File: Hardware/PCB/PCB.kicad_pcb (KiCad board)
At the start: 2 copper layers, 48 parts, among them IC1 MPXV6115VC6U, IC2 MPX5100GP, J3 Programmer, J4 Power Input, J5 Relay Terminal, Q1 MMBT2222A, SW2 RotaryEncoder_Switch_MP, U2 ADS1219IPWR, U3 LP3987H-33B5, U5 R-78E5.0-1.0, U6 AP7361C-33E, U7 DS3232M, U8 DRV8871DDA

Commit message: overall design is pretty much done, starting layout and routing now
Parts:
- removed R6: 10k, Resistor_SMD:R_0603_1608Metric_Pad0.98x0.95mm_HandSolder
- added C16: 10u, Capacitor_SMD:C_0805_2012Metric_Pad1.18x1.45mm_HandSolder, F.Cu at (-68.1, 57.1)
- added C23: 0.1uF, Capacitor_SMD:C_0603_1608Metric_Pad1.08x0.95mm_HandSolder, F.Cu at (-63.5, 56.9)
- added C24: 0.1u, Capacitor_SMD:C_0603_1608Metric_Pad1.08x0.95mm_HandSolder, F.Cu at (205.5, 86.0)
- added C31: 1uF, Capacitor_SMD:C_0603_1608Metric_Pad1.08x0.95mm_HandSolder, F.Cu at (-69.0, 25.1)
- added C32: 1uF, Capacitor_SMD:C_0603_1608Metric_Pad1.08x0.95mm_HandSolder, F.Cu at (-69.0, 27.6)
- added C33: 10u, Capacitor_SMD:C_0805_2012Metric_Pad1.18x1.45mm_HandSolder, F.Cu at (-101.5, 92.5)
- added C34: 10u, Capacitor_SMD:C_0805_2012Metric_Pad1.18x1.45mm_HandSolder, F.Cu at (-80.1, 71.9)
- added C35: 0.1u, Capacitor_SMD:C_0603_1608Metric_Pad1.08x0.95mm_HandSolder, F.Cu at (-84.7, 73.7)
- added C36: 0.1u, Capacitor_SMD:C_0603_1608Metric_Pad1.08x0.95mm_HandSolder, F.Cu at (-84.7, 76.2)
- added C39: 10uF, Capacitor_SMD:C_1206_3216Metric_Pad1.33x1.80mm_HandSolder, F.Cu at (208.9, 48.0)
- added C40: 0.1uF, Capacitor_SMD:C_0603_1608Metric_Pad1.08x0.95mm_HandSolder, F.Cu at (206.9, 48.7)
- added C41: 22uF, Capacitor_SMD:C_0805_2012Metric_Pad1.18x1.45mm_HandSolder, F.Cu at (200.6, 53.3)
- added C42: 22uF, Capacitor_SMD:C_0805_2012Metric_Pad1.18x1.45mm_HandSolder, F.Cu at (198.4, 53.3)
- added C43: 10uF, Capacitor_SMD:C_1206_3216Metric_Pad1.33x1.80mm_HandSolder, F.Cu at (211.5, 48.0)
- added C44: 10uF, Capacitor_SMD:C_1206_3216Metric_Pad1.33x1.80mm_HandSolder, F.Cu at (214.0, 48.0)
- added D4: LED, LED_SMD:LED_0603_1608Metric_Pad1.05x0.95mm_HandSolder, F.Cu at (-96.8, 94.9)
- added D5: SMD110PL-TP, Diode_SMD:D_SOD-123F, F.Cu at (189.8, 100.1)
- added D6: SMD110PL-TP, Diode_SMD:D_SOD-123F, F.Cu at (185.0, 100.1)
- added D7: SMD110PL-TP, Diode_SMD:D_SOD-123F, F.Cu at (180.1, 100.1)
- added J1: DC Motor Terminal, Vendor_Footprints:TE_1985218, F.Cu at (215.6, 65.5)
- added J18: Programmer, Vendor_Footprints:61200621621, F.Cu at (-95.4, 72.8)
- added J2: Solenoid Terminal, Vendor_Footprints:PHX_16PIN_1985292, F.Cu at (181.4, 105.7)
- added PS1: TPSM84338RCJR, Vendor_Footprints:CONV_TPSM84338RCJR, F.Cu at (203.9, 50.8)
- added Q2: MMBT2222A, Package_TO_SOT_SMD:SOT-23, F.Cu at (199.4, 96.9)
- added Q3: MMBT2222A, Package_TO_SOT_SMD:SOT-23, F.Cu at (194.6, 96.9)
- added Q4: MMBT2222A, Package_TO_SOT_SMD:SOT-23, F.Cu at (189.8, 96.9)
- added Q5: MMBT2222A, Package_TO_SOT_SMD:SOT-23, F.Cu at (185.0, 96.9)
- added Q6: MMBT2222A, Package_TO_SOT_SMD:SOT-23, F.Cu at (180.1, 96.9)
- added R11: 300, Resistor_SMD:R_0603_1608Metric_Pad0.98x0.95mm_HandSolder, F.Cu at (-69.0, 32.6)
- added R12: 4.7k, Resistor_SMD:R_0603_1608Metric_Pad0.98x0.95mm_HandSolder, F.Cu at (-69.0, 35.1)
- added R13: 470, Resistor_SMD:R_0603_1608Metric_Pad0.98x0.95mm_HandSolder, F.Cu at (198.4, 93.0)
- added R14: 10k, Resistor_SMD:R_0603_1608Metric_Pad0.98x0.95mm_HandSolder, F.Cu at (200.5, 93.0)
- added R15: 18k, Resistor_SMD:R_1206_3216Metric_Pad1.30x1.75mm_HandSolder, F.Cu at (189.0, 78.8)
- added R16: 470, Resistor_SMD:R_0603_1608Metric_Pad0.98x0.95mm_HandSolder, F.Cu at (193.6, 93.0)
- added R17: 10k, Resistor_SMD:R_0603_1608Metric_Pad0.98x0.95mm_HandSolder, F.Cu at (195.6, 93.0)
- added R18: 470, Resistor_SMD:R_0603_1608Metric_Pad0.98x0.95mm_HandSolder, F.Cu at (188.8, 93.0)
- added R19: 10k, Resistor_SMD:R_0603_1608Metric_Pad0.98x0.95mm_HandSolder, F.Cu at (190.8, 93.0)
- added R20: 470, Resistor_SMD:R_0603_1608Metric_Pad0.98x0.95mm_HandSolder, F.Cu at (183.9, 93.0)
- added R21: 10k, Resistor_SMD:R_0603_1608Metric_Pad0.98x0.95mm_HandSolder, F.Cu at (186.0, 93.0)
- added R22: 470, Resistor_SMD:R_0603_1608Metric_Pad0.98x0.95mm_HandSolder, F.Cu at (179.1, 93.0)
- added R23: 10k, Resistor_SMD:R_0603_1608Metric_Pad0.98x0.95mm_HandSolder, F.Cu at (181.1, 93.0)
- added R24: 82k, Capacitor_SMD:C_0603_1608Metric_Pad1.08x0.95mm_HandSolder, F.Cu at (199.8, 50.5)
- added R7: 470, Resistor_SMD:R_0603_1608Metric_Pad0.98x0.95mm_HandSolder, F.Cu at (-101.7, 95.2)
- added R9: 10k, Capacitor_SMD:C_0603_1608Metric_Pad1.08x0.95mm_HandSolder, F.Cu at (199.3, 48.7)
- added U1: ER-TFTM032-3, Vendor_Footprints:GCT_FFC3B07-40-T, F.Cu at (-46.2, 50.9)
- added U10: AZ1117-5.0, Package_TO_SOT_SMD:SOT-223-3_TabPin2, F.Cu at (-94.1, 86.2)
- added U11: ESP32-S3-WROOM-1U-N16R8, Vendor_Footprints:XCVR_ESP32-S3-WROOM-1U-N16R8, F.Cu at (-92.7, 56.5)
- added U9: TLV75533PDRV, Package_SON:WSON-6-1EP_2x2mm_P0.65mm_EP1x1.6mm, F.Cu at (-91.0, 92.1)
- C10: value 10uF -> 0.1u; footprint Capacitor_SMD:C_0805_2012Metric -> Capacitor_SMD:C_0603_1608Metric_Pad1.08x0.95mm_HandSolder
- C11: value 0.1uF -> 0.1u; footprint Capacitor_SMD:C_0805_2012Metric_Pad1.18x1.45mm_HandSolder -> Capacitor_SMD:C_0603_1608Metric_Pad1.08x0.95mm_HandSolder
- C12: value 1uF -> 22uF; footprint Capacitor_SMD:C_0603_1608Metric_Pad1.08x0.95mm_HandSolder -> Capacitor_SMD:CP_Elec_8x10
- C13: value 1uF -> 0.1uF; footprint Capacitor_SMD:C_0603_1608Metric_Pad1.08x0.95mm_HandSolder -> Capacitor_SMD:C_1206_3216Metric_Pad1.33x1.80mm_HandSolder
- C14: value 1uF -> 22uF; footprint Capacitor_SMD:C_0805_2012Metric_Pad1.18x1.45mm_HandSolder -> Capacitor_SMD:CP_Elec_8x10
- C15: footprint Capacitor_SMD:C_0603_1608Metric_Pad1.08x0.95mm_HandSolder -> Capacitor_SMD:C_1206_3216Metric_Pad1.33x1.80mm_HandSolder
- C7: value 22uF -> 1u; footprint Capacitor_THT:CP_Radial_D10.0mm_P5.00mm -> Capacitor_SMD:C_0603_1608Metric_Pad1.08x0.95mm_HandSolder
- C8: value 0.1uF -> 0.1u
- C9: value 10uF -> 10u; footprint Capacitor_SMD:C_0805_2012Metric -> Capacitor_SMD:C_0805_2012Metric_Pad1.18x1.45mm_HandSolder
- D1, D2: value BAT60AE6327HTSA1 -> SMD110PL-TP; footprint Diode_SMD:D_SOD-323_HandSoldering -> Diode_SMD:D_SOD-123F
- J3: value Programmer -> Brushless Pump Motor; footprint Vendor_Footprints:61200621621 -> Vendor_Footprints:TE_1985205
- J4: value Power Input -> 54-00127; footprint Vendor_Footprints:PHOENIX_1984963 -> Vendor_Footprints:TENSILITY_54-00127
- J5: value Relay Terminal -> Brushless Vacuum Motor; footprint Vendor_Footprints:PHOENIX_1984963 -> Vendor_Footprints:TE_1985205
- R3: value 1k -> 470
- SW2: value RotaryEncoder_Switch_MP -> ~; footprint Rotary_Encoder:RotaryEncoder_Alps_EC11E-Switch_Vertical_H20mm_CircularMountingHoles -> Vendor_Footprints:PTS647SN50SMTR2LFS
- U3: value LP3987H-33B5 -> DRV8871DDA; footprint Package_TO_SOT_SMD:TO-263-5_TabPin3 -> Package_SO:Texas_HTSOP-8-1EP_3.9x4.9mm_P1.27mm_EP2.95x4.9mm_Mask2.4x3.1mm_ThermalVias
- U5: value R-78E5.0-1.0 -> 74LVC2T45DC; footprint Converter_DCDC:Converter_DCDC_RECOM_R-78E-0.5_THT -> Package_SO:VSSOP-8_2.3x2mm_P0.5mm
- U6: value AP7361C-33E -> TPS7A2050PDBVR; footprint Package_TO_SOT_SMD:SOT-223-3_TabPin2 -> Package_TO_SOT_SMD:SOT-23-5
- moved C8 214.2 mm to (-84.7, 71.2)
- moved C7 205.2 mm to (-84.7, 68.7)
- moved U2 203.3 mm to (-99.0, 40.9)
- moved R2 196.7 mm to (-84.7, 78.7)
- moved C9 191.8 mm to (-80.1, 68.9)
- moved C18 186.1 mm to (-101.5, 83.5)
- moved C19 186.1 mm to (-101.5, 86.5)
- moved C20 186.1 mm to (-101.5, 89.5)
- moved U6 185.7 mm to (-92.0, 40.0)
- moved SW1 181.5 mm to (-77.5, 50.0)
- moved SW2 180.2 mm to (-77.5, 57.6)
- moved TP1 180.0 mm to (-78.0, 26.4)
- moved TP2 180.0 mm to (-78.0, 31.4)
- moved TP3 180.0 mm to (-78.0, 36.5)
- moved BT1 179.3 mm to (-58.2, 69.2)
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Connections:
- C1 pad 2: +5V -> +5VA
- C10 pad 1: +3.3V -> Net-(PS1-SS/PG)
- C12 pad 1: GND -> +24V
- C12 pad 2: +5V -> GND
- C13 pad 1: GND -> +24V
- C13 pad 2: +4.7V -> GND
- C14 pad 1: /esp32/ESP-EN -> +24V
- C15 pad 1: Net-(C15-Pad1) -> +24V
- C15 pad 2: Net-(C15-Pad2) -> GND
- C17 pad 1: VCC -> +5.5V
- C18 pad 1: Net-(D2-A) -> +5V
- C2 pad 2: +5V -> +5VA
- C5 pad 2: +5V -> +5VA
- C6 pad 2: +5V -> +5VA
- C7 pad 1: Vdrive -> GND
- C7 pad 2: GND2 -> /ESP32-S3/EN
- C8 pad 1: Vdrive -> GND
- C8 pad 2: GND2 -> +3.3V
- C9 pad 1: +3.3V -> GND
- C9 pad 2: GND -> +3.3V
- D1 pad 1: +5V -> +24V
- D1 pad 2: Net-(D1-A) -> /relay_driver1/COIL-
- D2 pad 1: +5V -> +24V
- D2 pad 2: Net-(D2-A) -> /relay_driver2/COIL-
- D3 pad 1: VCC -> +24V
- D3 pad 2: Net-(D3-A) -> /relay_driver/COIL-
- IC1 pad 2: +5V -> +5VA
- IC2 pad 3: +5V -> +5VA
- J3 pad 1: /esp32/ESP-EN -> +24V
- J3 pad 2: Net-(D1-A) -> /brushless_motor_pwm_driver/BRUSHLESS_PWM_1
- J3 pad 3: /esp32/ESP-TX -> GND
- J5 pad 1: VCC -> +24V
- J5 pad 2: Net-(D3-A) -> /brushless_motor_pwm_driver/BRUSHLESS_PWM_2
- Q1 pad 3: Net-(D3-A) -> /relay_driver/COIL-
- R2 pad 1: /esp32/D12 -> +3.3V
- R2 pad 2: GND -> /ESP32-S3/EN
- R3 pad 1: /relay_driver/RELAY-COIL-SIGNAL -> /SOLENOID_1
- R5 pad 2: GND2 -> GND
- SW1 pad 1: /esp32/ESP-EN -> /ESP32-S3/EN
- SW1 pad 2: Net-(C15-Pad1) -> Net-(C35-Pad1)
- SW1 pad 4: Net-(C15-Pad2) -> Net-(C35-Pad2)
- U2 pad 14: /sensors//DRDY -> /ADC-DRDY
- U2 pad 15: /sensors/SDA -> /I2C-SDA
- U2 pad 16: /sensors/SCL -> /I2C-SCL
- U2 pad 3: /sensors//RESET -> /ADC-RESET
- U3 pad 1: +5V -> GND
- U3 pad 2: GND -> /PUMP-IN2
- U3 pad 3: +5V -> /PUMP-IN1
- U3 pad 4: unconnected-(U3-NC-Pad4) -> Net-(U3-ILIM)
- U3 pad 5: +4.7V -> +24V
- U5 pad 1: VCC -> +5V
- U5 pad 2: GND -> /brushless_motor_pwm_driver/BRUSHLESS_PWM_1
- U5 pad 3: Net-(D2-A) -> /brushless_motor_pwm_driver/BRUSHLESS_PWM_2
- U6 pad 1: +5V -> +5.5V
- U6 pad 3: +3.3V -> +5.5V
- U7 pad 3: /rtc//INT -> /RTC-INT
- U7 pad 4: /rtc//RST -> /RTC-RESET
- U7 pad 7: /rtc/SDA -> /I2C-SDA
- U7 pad 8: /rtc/SCL -> /I2C-SCL
- U8 pad 1: GND2 -> GND
- U8 pad 2: /motor_driver/IN2 -> /VAC-IN2
- U8 pad 3: /motor_driver/IN1 -> /VAC-IN1
- U8 pad 5: Vdrive -> +24V
- U8 pad 6: Net-(J6-Pin_1) -> /motor_driver/MOTOR-OUT-1
- U8 pad 7: GND2 -> GND
- U8 pad 8: Net-(J6-Pin_2) -> /motor_driver/MOTOR-OUT-2
- U8 pad 9: GND2 -> GND
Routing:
- net /motor_driver/MOTOR-OUT-2: track 0.00 -> 26.9 mm
- net /motor_driver1/MOTOR-OUT-2: track 0.00 -> 26.3 mm
- net /motor_driver1/MOTOR-OUT-1: track 0.00 -> 22.5 mm
- net /motor_driver/MOTOR-OUT-1: track 0.00 -> 18.8 mm
- net /relay_driver/COIL-: track 0.00 -> 16.0 mm
- net /relay_driver1/COIL-: track 0.00 -> 14.6 mm
- net /relay_driver2/COIL-: track 0.00 -> 12.1 mm
- net /relay_driver3/COIL-: track 0.00 -> 10.3 mm
- net /relay_driver4/COIL-: track 0.00 -> 9.35 mm
- net /relay_driver5/COIL-: track 0.00 -> 8.55 mm
- net Net-(Q4-B): track 0.00 -> 4.10 mm
- net Net-(Q3-B): track 0.00 -> 4.10 mm
- net Net-(Q2-B): track 0.00 -> 4.10 mm
- net Net-(Q1-B): track 0.00 -> 4.10 mm
- net Net-(Q6-B): track 0.00 -> 4.10 mm
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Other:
- board outline added: 1.8 x 1.8 mm

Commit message: pcb layout and routing pretty much done, checking DRC
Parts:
- removed C1: 0.01uF, Capacitor_SMD:C_0603_1608Metric_Pad1.08x0.95mm_HandSolder
- removed C18, C33: 10u, Capacitor_SMD:C_0805_2012Metric_Pad1.18x1.45mm_HandSolder
- removed C2, C5: 1uF, Capacitor_SMD:C_0603_1608Metric_Pad1.08x0.95mm_HandSolder
- removed C3: 470p, Capacitor_SMD:C_0603_1608Metric_Pad1.08x0.95mm_HandSolder
- removed C4: 47pF, Capacitor_SMD:C_0603_1608Metric_Pad1.08x0.95mm_HandSolder
- removed C6: 100nF, Capacitor_SMD:C_0603_1608Metric_Pad1.08x0.95mm_HandSolder
- removed IC1: MPXV6115VC6U, Vendor_Footprints:MPXV6115VC6U
- removed IC2: MPX5100GP, Vendor_Footprints:MPX5100GP
- removed R1: 51k, Resistor_SMD:R_0603_1608Metric_Pad0.98x0.95mm_HandSolder
- removed TP1, TP2: TestPoint_Probe, TestPoint:TestPoint_Keystone_5010-5014_Multipurpose
- removed U9: TLV75533PDRV, Package_SON:WSON-6-1EP_2x2mm_P0.65mm_EP1x1.6mm
- added C25: 10u, Capacitor_SMD:C_0805_2012Metric_Pad1.18x1.45mm_HandSolder, F.Cu at (153.9, 93.7)
- added C26: 10u, Capacitor_SMD:C_0805_2012Metric_Pad1.18x1.45mm_HandSolder, F.Cu at (143.2, 101.1)
- added C27: 10u, Capacitor_SMD:C_0805_2012Metric_Pad1.18x1.45mm_HandSolder, F.Cu at (143.2, 105.1)
- added C28: 470pF, Capacitor_SMD:C_0603_1608Metric_Pad1.08x0.95mm_HandSolder, F.Cu at (148.6, 125.3)
- added C29: 1uF, Capacitor_SMD:C_0603_1608Metric_Pad1.08x0.95mm_HandSolder, F.Cu at (148.6, 121.7)
- added C30: 0.01uF, Capacitor_SMD:C_0402_1005Metric_Pad0.74x0.62mm_HandSolder, F.Cu at (150.1, 121.5)
- added C37: 0.33uF, Capacitor_SMD:C_0603_1608Metric_Pad1.08x0.95mm_HandSolder, F.Cu at (131.5, 124.1)
- added C38: 0.33uF, Capacitor_SMD:C_0603_1608Metric_Pad1.08x0.95mm_HandSolder, F.Cu at (151.4, 124.3)
- added C45: 22uF, Capacitor_SMD:C_0805_2012Metric_Pad1.18x1.45mm_HandSolder, F.Cu at (138.4, 71.4)
- added C46: 0.1u, Capacitor_SMD:C_0603_1608Metric_Pad1.08x0.95mm_HandSolder, F.Cu at (127.4, 95.0)
- added C47: 22uF, Capacitor_SMD:C_0805_2012Metric_Pad1.18x1.45mm_HandSolder, F.Cu at (142.2, 93.3)
- added H1: MountingHole, MountingHole:MountingHole_3.2mm_M3, F.Cu at (108.2, 126.5)
- added H3: MountingHole, MountingHole:MountingHole_3.2mm_M3, F.Cu at (227.9, 129.0)
- added H4: MountingHole, MountingHole:MountingHole_3.2mm_M3, F.Cu at (114.6, 81.5)
- added IC3: MPX5500DP, Vendor_Footprints:MPX5500DP, F.Cu at (121.2, 129.8)
- added IC4: MPX5500DP, Vendor_Footprints:MPX5500DP, F.Cu at (141.1, 129.8)
- added NT1: NetTie_2, NetTie:NetTie-2_SMD_Pad0.5mm, F.Cu at (135.6, 100.8)
- added R25: 750, Resistor_SMD:R_0603_1608Metric_Pad0.98x0.95mm_HandSolder, F.Cu at (131.5, 125.8)
- added R26: 750, Resistor_SMD:R_0603_1608Metric_Pad0.98x0.95mm_HandSolder, F.Cu at (151.4, 126.0)
- added TP4: TestPoint_Probe, TestPoint:TestPoint_Keystone_5000-5004_Miniature, F.Cu at (123.7, 104.1)
- added TP5: TestPoint_Probe, TestPoint:TestPoint_Keystone_5000-5004_Miniature, F.Cu at (114.6, 104.1)
- added TP6: TestPoint_Probe, TestPoint:TestPoint_Keystone_5000-5004_Miniature, F.Cu at (128.3, 104.1)
- added U4: AP7361C-33E, Package_TO_SOT_SMD:SOT-223-3_TabPin2, F.Cu at (148.8, 103.1)
- C17: value 10u -> 1uF; footprint Capacitor_SMD:C_1206_3216Metric_Pad1.33x1.80mm_HandSolder -> Capacitor_SMD:C_0603_1608Metric_Pad1.08x0.95mm_HandSolder
- C19: value 10u -> 0.01uF; footprint Capacitor_SMD:C_0805_2012Metric_Pad1.18x1.45mm_HandSolder -> Capacitor_SMD:C_0402_1005Metric_Pad0.74x0.62mm_HandSolder
- C20: value 10u -> 470pF; footprint Capacitor_SMD:C_0805_2012Metric_Pad1.18x1.45mm_HandSolder -> Capacitor_SMD:C_0603_1608Metric_Pad1.08x0.95mm_HandSolder
- C34, C9: value 10u -> 0.1u; footprint Capacitor_SMD:C_0805_2012Metric_Pad1.18x1.45mm_HandSolder -> Capacitor_SMD:C_0603_1608Metric_Pad1.08x0.95mm_HandSolder
- J3: value Brushless Pump Motor -> Brushless Vac Motor
- J5: value Brushless Vacuum Motor -> Brushless Pump Motor
- TP3: footprint TestPoint:TestPoint_Keystone_5010-5014_Multipurpose -> TestPoint:TestPoint_Keystone_5000-5004_Miniature
- moved J18 261.8 mm to (166.4, 78.7), turned to -90 degrees
- moved U11 243.8 mm to (150.1, 79.5)
- moved U10 242.4 mm to (148.1, 95.0), turned to 180 degrees
- moved R7 240.1 mm to (138.4, 95.0), turned to -90 degrees
- moved D4 237.1 mm to (140.2, 93.2), turned to 90 degrees
- moved U2 236.3 mm to (131.1, 95.0), turned to -90 degrees
- moved C19 234.3 mm to (130.2, 121.3), turned to -90 degrees
- moved C20 232.9 mm to (128.7, 125.1), turned to -90 degrees
- moved U7 232.6 mm to (165.0, 106.2)
- moved BT1 229.8 mm to (165.6, 121.2), turned to -90 degrees
- moved C17 226.7 mm to (128.7, 121.5), turned to -90 degrees
- moved C7 223.1 mm to (138.3, 76.5)
- moved R2 223.0 mm to (138.3, 74.7)
- moved C21 221.8 mm to (160.3, 105.6), turned to 90 degrees
- moved C8 221.1 mm to (136.4, 71.6), turned to -90 degrees
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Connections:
- C17 pad 1: +5.5V -> +5VA
- C17 pad 2: GND -> GNDA
- C19 pad 1: +5V -> +5VA
- C19 pad 2: GND -> GNDA
- C20 pad 1: +3.3V -> GNDA
- C20 pad 2: GND -> Net-(IC3-VOUT)
- C31 pad 1: GND -> GNDA
- C32 pad 1: GND -> GNDA
- C9 pad 1: GND -> GNDA
- J18 pad 2: +5V -> unconnected-(J18-Pin_2-Pad2)
- J4 pad SH1: (no net) -> GND
- J4 pad SH2: (no net) -> GND
- R12 pad 2: GND -> GNDA
- U1 pad S1: (no net) -> GND
- U1 pad S2: (no net) -> GND
- U11 pad 13: /RTC-INT -> /DISP-RESET
- U11 pad 14: /ADC-DRDY -> /ADC-RESET
- U11 pad 15: /RTC-INT -> /ADC-DRDY
- U11 pad 17: /DISP-RESET -> /ESP32-S3/GPIO9
- U11 pad 18: /DISP-CS -> /GPIO10
- U11 pad 22: /RTC-RESET -> /RTC-INT
- U11 pad 23: /ADC-RESET -> /RTC-RESET
- U11 pad 36: /GPIO44 -> /ESP32-S3/RX
- U11 pad 37: /GPIO43 -> /ESP32-S3/TX
- U11 pad 38: /PUMP-IN2 -> /VAC-IN1
- U11 pad 39: /PUMP-IN1 -> /VAC-IN2
- U11 pad 6: /TOUCH-CS -> /DISP-DC
- U11 pad 7: /DISP-DC -> /DISP-CS
- U11 pad 8: /VAC-IN1 -> /PUMP-IN2
- U11 pad 9: /VAC-IN2 -> /PUMP-IN1
- U2 pad 5: GND -> GNDA
- U2 pad 8: GND -> GNDA
- U5 pad 6: /VAC-IN1 -> /PUMP-IN1
- U5 pad 7: /PUMP-IN1 -> /VAC-IN1
- U6 pad 2: GND -> GNDA
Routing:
- net +5V: track 0.00 -> 188.0 mm, vias 0 -> 3
- net +3.3V: track 0.00 -> 153.4 mm, vias 0 -> 6
- net /I2C-SDA: track 0.00 -> 91.8 mm, vias 0 -> 4
- net /I2C-SCL: track 0.00 -> 88.1 mm, vias 0 -> 4
- net +5VA: track 0.00 -> 87.5 mm, vias 0 -> 3
- net /PUMP-IN1: track 0.00 -> 73.1 mm, vias 0 -> 2
- net +5.5V: track 0.00 -> 71.8 mm, vias 0 -> 3
- net /VAC-IN1: track 0.00 -> 69.2 mm
- net /SOLENOID_1: track 0.00 -> 66.5 mm, vias 0 -> 2
- net /SOLENOID_2: track 0.00 -> 63.9 mm, vias 0 -> 2
- net /SOLENOID_3: track 0.00 -> 61.3 mm, vias 0 -> 2
- net /SPI-CLK: track 0.00 -> 60.3 mm, vias 0 -> 3
- net /SOLENOID_4: track 0.00 -> 58.7 mm, vias 0 -> 2
- net /SPI-MOSI: track 0.00 -> 56.3 mm, vias 0 -> 2
- net /SOLENOID_5: track 0.00 -> 56.2 mm, vias 0 -> 2
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- added copper zone on B.Cu, net +24V
- added copper zone on F.Cu, net +24V
- added copper zone on B.Cu, net +5.5V
- added copper zone on F.Cu, net +5.5V
- added copper zone on B.Cu, net GND
- added copper zone on F.Cu, net GND
- added copper zone on In1.Cu, net GND
- added copper zone on In2.Cu, net GND
- added copper zone on F.Cu, net GNDA
- added copper zone on In1.Cu, net GNDA
- added copper zone on In2.Cu, net GNDA
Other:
- board size 1.8 x 1.8 mm -> 130 x 65 mm
- copper layers 2 -> 4
- board text added: "+ - CLAMP"
- board text added: "+ - VAC"
- board text added: "+ PWM - CLAMP BLDC"
- board text added: "+ PWM - VAC BLDC"
- board text added: "- + S1"
- board text added: "- + S2"
- board text added: "- + S3"
- board text added: "- + S4"
- board text added: "- + S5"
- board text added: "- + S6"
- board text added: "P1 (+)"
- board text added: "P2 (-)"
- board text added: "PUMP"
- board text added: "VAC"

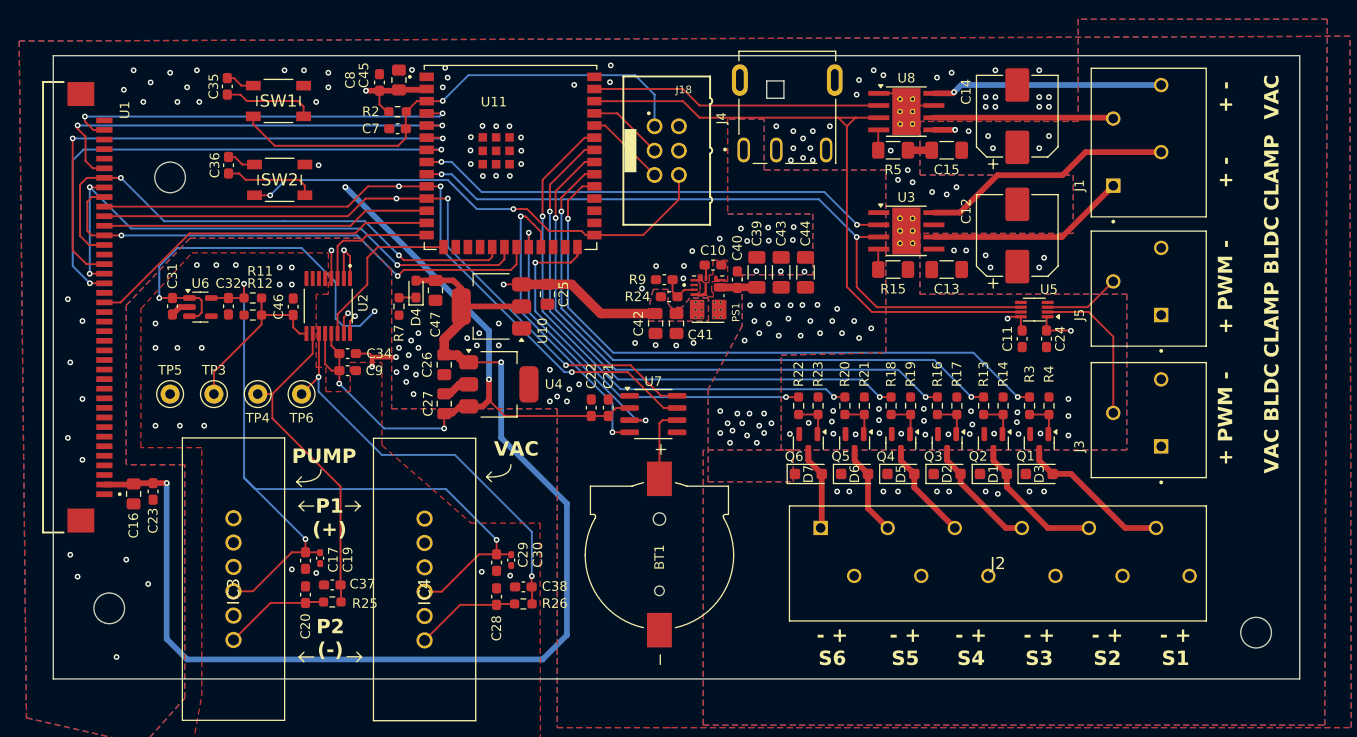
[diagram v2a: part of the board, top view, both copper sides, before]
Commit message: fixed BOM, added some silkscreen, getting quote now
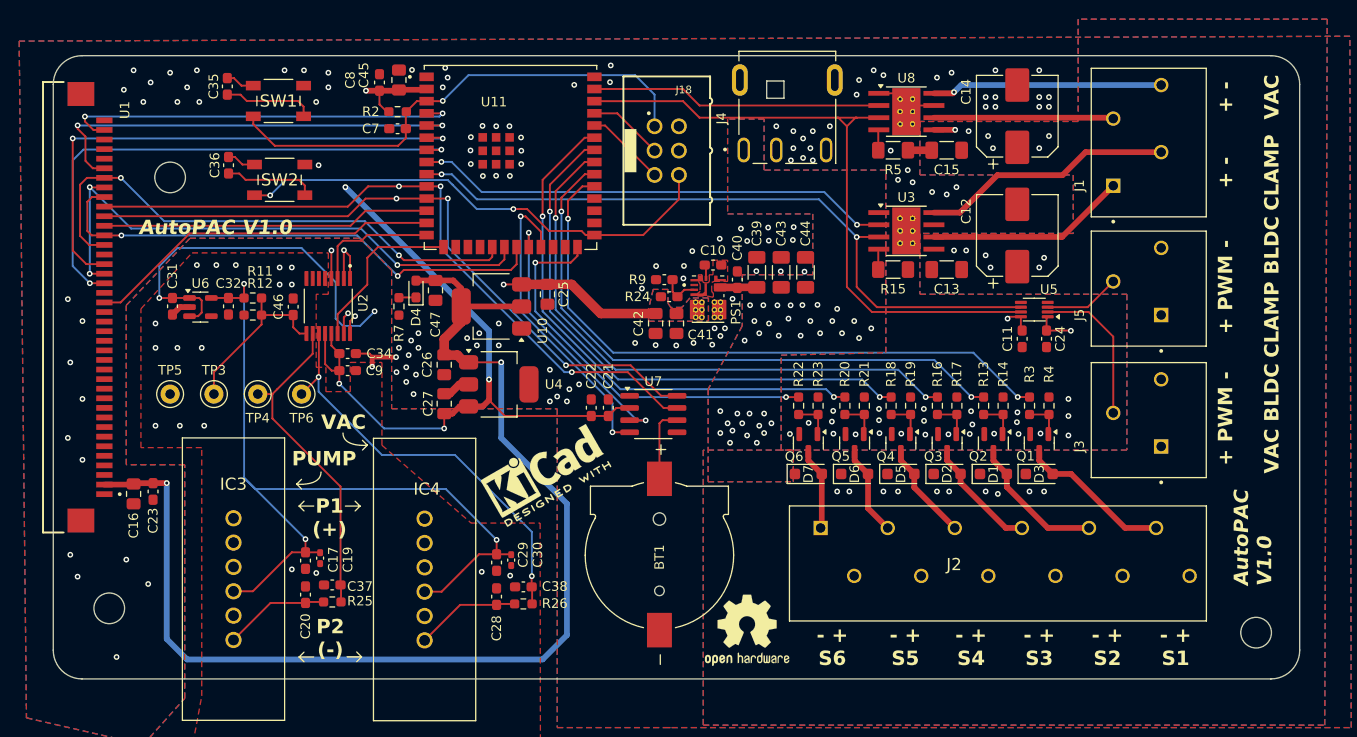
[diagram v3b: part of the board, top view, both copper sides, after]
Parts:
- added REF**: OSHW-Logo2_9.8x8mm_SilkScreen, Symbol:OSHW-Logo2_9.8x8mm_SilkScreen, F.Cu at (174.8, 128.8)
- added REF**: KiCad-Logo2_5mm_SilkScreen, Symbol:KiCad-Logo2_5mm_SilkScreen, F.Cu at (153.7, 112.3)
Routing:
- net GND: vias 146 -> 151
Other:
- outline, holes or cut-outs redrawn
- board text added: "AutoPAC V1.0"

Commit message: done with this, placed order
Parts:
- removed BT1: 1056, Vendor_Footprints:BAT_1056
- removed C29: 1uF, Capacitor_SMD:C_0603_1608Metric_Pad1.08x0.95mm_HandSolder
- removed C30: 0.01uF, Capacitor_SMD:C_0402_1005Metric_Pad0.74x0.62mm_HandSolder
- removed C34, C35, C36, C46, C9: 0.1u, Capacitor_SMD:C_0603_1608Metric_Pad1.08x0.95mm_HandSolder
- removed C43, C44: 10uF, Capacitor_SMD:C_1206_3216Metric_Pad1.33x1.80mm_HandSolder
- removed D1, D2, D3, D5, D6, D7: SMD110PL-TP, Diode_SMD:D_SOD-123F
- removed D4: LED, LED_SMD:LED_0603_1608Metric_Pad1.05x0.95mm_HandSolder
- removed H3: MountingHole, MountingHole:MountingHole_3.2mm_M3
- removed J5: Brushless Pump Motor, Vendor_Footprints:TE_1985205
- removed PS1: TPSM84338RCJR, Vendor_Footprints:CONV_TPSM84338RCJR
- removed R24: 82k, Capacitor_SMD:C_0603_1608Metric_Pad1.08x0.95mm_HandSolder
- removed R9: 10k, Capacitor_SMD:C_0603_1608Metric_Pad1.08x0.95mm_HandSolder
- removed SW1, SW2: ~, Vendor_Footprints:PTS647SN50SMTR2LFS
- removed TP5: TestPoint_Probe, TestPoint:TestPoint_Keystone_5000-5004_Miniature
- removed U5: 74LVC2T45DC, Package_SO:VSSOP-8_2.3x2mm_P0.5mm
- removed U7: DS3232M, Package_SO:SOIC-8_3.9x4.9mm_P1.27mm
- added C18: 100nF, Capacitor_SMD:C_0603_1608Metric_Pad1.08x0.95mm_HandSolder, F.Cu at (187.7, 49.8)
- added C48: 47uF, Capacitor_SMD:C_1210_3225Metric, F.Cu at (192.3, 52.8)
- added C49: 47uF, Capacitor_SMD:C_1210_3225Metric, F.Cu at (192.3, 56.6)
- added C50: 22uF, Capacitor_SMD:C_0805_2012Metric_Pad1.18x1.45mm_HandSolder, F.Cu at (211.1, 42.7)
- added D10: SS310, Diode_SMD:D_SMA, F.Cu at (260.6, 53.4)
- added D11: SS310, Diode_SMD:D_SMA, F.Cu at (260.6, 63.0)
- added D12: SS310, Diode_SMD:D_SMA, F.Cu at (260.6, 72.6)
- added D13: SS310, Diode_SMD:D_SMA, F.Cu at (260.6, 82.2)
- added D14: SS310, Diode_SMD:D_SMA, F.Cu at (260.6, 91.9)
- added D8: SS310, Diode_SMD:D_SMA, F.Cu at (187.7, 54.8)
- added D9: SS310, Diode_SMD:D_SMA, F.Cu at (260.6, 43.7)
- added H2: MountingHole, MountingHole:MountingHole_3.2mm_M3, F.Cu at (221.5, 52.6)
- added J13: Solenoid Terminal, Vendor_Footprints:CONN_WJ15EDGRC-3.81-2P, F.Cu at (264.5, 51.6)
- added J14: Solenoid Terminal, Vendor_Footprints:CONN_WJ15EDGRC-3.81-2P, F.Cu at (264.5, 61.2)
- added J15: Solenoid Terminal, Vendor_Footprints:CONN_WJ15EDGRC-3.81-2P, F.Cu at (264.5, 70.8)
- added J16: Solenoid Terminal, Vendor_Footprints:CONN_WJ15EDGRC-3.81-2P, F.Cu at (264.5, 80.4)
- added J17: Solenoid Terminal, Vendor_Footprints:CONN_WJ15EDGRC-3.81-2P, F.Cu at (264.5, 90.1)
- added J6: XUNPU DC-005-A250, Connector_BarrelJack:BarrelJack_Horizontal, F.Cu at (192.5, 41.6)
- added J7: Solenoid Terminal, Vendor_Footprints:CONN_WJ15EDGRC-3.81-2P, F.Cu at (264.5, 41.9)
- added L1: 6.8uH, Inductor_SMD:L_Changjiang_FXL0630, F.Cu at (190.8, 62.4)
- added R10: 66.5k, Capacitor_SMD:C_0603_1608Metric_Pad1.08x0.95mm_HandSolder, F.Cu at (181.9, 59.1)
- added R27: 10.5k, Capacitor_SMD:C_0603_1608Metric_Pad1.08x0.95mm_HandSolder, F.Cu at (181.9, 57.4)
- added R28: 45.3k, Capacitor_SMD:C_0603_1608Metric_Pad1.08x0.95mm_HandSolder, F.Cu at (180.2, 48.1)
- added R6: 2.2k, Resistor_SMD:R_0603_1608Metric_Pad0.98x0.95mm_HandSolder, F.Cu at (242.6, 81.3)
- added REF**: Fiducial_1mm_Mask3mm, Fiducial:Fiducial_1mm_Mask3mm, F.Cu at (180.8, 41.4)
- added REF**: Fiducial_1mm_Mask3mm, Fiducial:Fiducial_1mm_Mask3mm, F.Cu at (256.3, 34.8)
- added REF**: Fiducial_1mm_Mask3mm, Fiducial:Fiducial_1mm_Mask3mm, F.Cu at (214.6, 95.2)
- added U12: AZ1117-3.3, Package_TO_SOT_SMD:SOT-223-3_TabPin2, F.Cu at (211.1, 49.6)
- added U9: LMR16030PDDAR, Vendor_Footprints:VREG_LM5017MR_NOPB, F.Cu at (183.0, 52.7)
- C10, C11, C24, C8: value 0.1u -> 100nF
- C13, C15: value 0.1uF -> 100nF; footprint Capacitor_SMD:C_1206_3216Metric_Pad1.33x1.80mm_HandSolder -> Capacitor_SMD:C_0603_1608Metric_Pad1.08x0.95mm_HandSolder
- C16: value 10u -> 10uF; footprint Capacitor_SMD:C_0805_2012Metric_Pad1.18x1.45mm_HandSolder -> Capacitor_SMD:C_0603_1608Metric_Pad1.08x0.95mm_HandSolder; moved to B.Cu
- C21: value 1uF -> 470pF
- C22: value 0.1uF -> 1uF
- C23: value 0.1uF -> 100nF; moved to B.Cu
- C25, C26: value 10u -> 10uF; footprint Capacitor_SMD:C_0805_2012Metric_Pad1.18x1.45mm_HandSolder -> Capacitor_SMD:C_0603_1608Metric_Pad1.08x0.95mm_HandSolder
- C27: value 10u -> 0.01uF; footprint Capacitor_SMD:C_0805_2012Metric_Pad1.18x1.45mm_HandSolder -> Capacitor_SMD:C_0402_1005Metric_Pad0.74x0.62mm_HandSolder
- C28: value 470pF -> 0.01uF; footprint Capacitor_SMD:C_0603_1608Metric_Pad1.08x0.95mm_HandSolder -> Capacitor_SMD:C_0402_1005Metric_Pad0.74x0.62mm_HandSolder
- C31, C32: value 1uF -> 100nF
- C40: value 0.1uF -> 100nF
- C41, C42: value 22uF -> 1uF; footprint Capacitor_SMD:C_0805_2012Metric_Pad1.18x1.45mm_HandSolder -> Capacitor_SMD:C_0603_1608Metric_Pad1.08x0.95mm_HandSolder
- C7: value 1u -> 1uF
- J1: value DC Motor Terminal -> Pump Motor; footprint Vendor_Footprints:TE_1985218 -> Vendor_Footprints:CONN_WJ15EDGRC-3.81-2P
- J2: value Solenoid Terminal -> Pump Motor; footprint Vendor_Footprints:PHX_16PIN_1985292 -> Vendor_Footprints:CONN_WJ15EDGRC-3.81-2P
- J3: value Brushless Vac Motor -> BLDC Motor; footprint Vendor_Footprints:TE_1985205 -> Vendor_Footprints:CONN_WJ15EDGRC-3.81-3P
- J4: value 54-00127 -> BLDC Motor; footprint Vendor_Footprints:TENSILITY_54-00127 -> Vendor_Footprints:CONN_WJ15EDGRC-3.81-3P
- R15, R5: footprint Resistor_SMD:R_1206_3216Metric_Pad1.30x1.75mm_HandSolder -> Resistor_SMD:R_0805_2012Metric_Pad1.20x1.40mm_HandSolder
- R7: value 470 -> 2.2k
- U1: moved to B.Cu
- U2: value ADS1219IPWR -> SN74LVC2T45DCUR; footprint Vendor_Footprints:SOP65P640X120-16N -> Package_SO:VSSOP-8_2.3x2mm_P0.5mm
- U4: value AP7361C-33E -> SPX5205M5-L-5-0/TR; footprint Package_TO_SOT_SMD:SOT-223-3_TabPin2 -> Package_TO_SOT_SMD:SOT-23-5
- U6: value TPS7A2050PDBVR -> ADS1232IPW; footprint Package_TO_SOT_SMD:SOT-23-5 -> Package_SO:TSSOP-24_6.1x7.8mm_P0.65mm
- moved H4 157.9 mm to (265.4, 34.8)
- moved U1 133.3 mm to (238.6, 92.9), turned to 180 degrees
- moved H1 117.5 mm to (181.6, 34.8)
- moved C16 114.2 mm to (221.7, 87.5), turned to -90 degrees
- moved C23 110.6 mm to (220.1, 87.5), turned to -90 degrees
- moved R2 110.4 mm to (247.6, 90.6), turned to 180 degrees
- moved C45 107.7 mm to (243.7, 94.0), turned to 90 degrees
- moved C8 107.7 mm to (241.7, 93.8), turned to 90 degrees
- moved C7 107.6 mm to (245.0, 89.7), turned to -90 degrees
- moved R7 104.8 mm to (242.5, 83.0), turned to 180 degrees
- moved U2 101.8 mm to (218.5, 42.7)
- moved J2 101.7 mm to (242.1, 35.8)
- moved REF** 97.7 mm to (240.5, 67.6), turned to 0 degrees
- moved C47 83.6 mm to (208.8, 42.7), turned to 90 degrees
- moved C31 82.4 mm to (194.5, 74.0)
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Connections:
- net /ESP32-S3/GPIO9 renamed /GPIO9
- C10 pad 1: Net-(PS1-SS/PG) -> Net-(C10-Pad1)
- C10 pad 2: GND -> Net-(C10-Pad2)
- C21 pad 1: +3.3V -> GNDA
- C21 pad 2: GND -> Net-(IC4-VOUT)
- C22 pad 1: GND -> +5VA
- C22 pad 2: +3.3V -> GNDA
- C27 pad 1: +3.3V -> GNDA
- C27 pad 2: GND -> Net-(U4-BP)
- C28 pad 1: GNDA -> +5VA
- C28 pad 2: Net-(IC4-VOUT) -> GNDA
- C31 pad 1: GNDA -> +5VA
- C31 pad 2: +5.5V -> GNDA
- C32 pad 1: GNDA -> +3.3V
- C32 pad 2: +5VA -> GND
- C37 pad 2: /sensors/CLAMP_SENSOR -> /sensors/pressure_sensor/SENSOR_VOUT
- C38 pad 2: /sensors/VAC_SENSOR -> /sensors/pressure_sensor1/SENSOR_VOUT
- C41 pad 1: +5.5V -> GNDA
- C41 pad 2: GND -> +5VA
- C42 pad 1: +5.5V -> GND
- C42 pad 2: GND -> +5.5V
- J1 pad 1: /motor_driver1/MOTOR-OUT-1 -> Net-(J1-Pin_1)
- J1 pad 2: /motor_driver1/MOTOR-OUT-2 -> Net-(J1-Pin_2)
- J2 pad 1: /relay_driver5/COIL- -> Net-(J2-Pin_1)
- J2 pad 2: +24V -> Net-(J2-Pin_2)
- J3 pad 2: /brushless_motor_pwm_driver/BRUSHLESS_PWM_1 -> Net-(J3-Pin_2)
- Q1 pad 3: /relay_driver/COIL- -> Net-(D9-A)
- Q2 pad 3: /relay_driver1/COIL- -> Net-(D10-A)
- Q3 pad 3: /relay_driver2/COIL- -> Net-(D11-A)
- Q4 pad 3: /relay_driver3/COIL- -> Net-(D12-A)
- Q5 pad 3: /relay_driver4/COIL- -> Net-(D13-A)
- Q6 pad 3: /relay_driver5/COIL- -> Net-(D14-A)
- R25 pad 2: /sensors/CLAMP_SENSOR -> /sensors/pressure_sensor/SENSOR_VOUT
- R26 pad 2: /sensors/VAC_SENSOR -> /sensors/pressure_sensor1/SENSOR_VOUT
- R7 pad 1: Net-(D4-K) -> +3.3V
- R7 pad 2: GND -> /I2C-SDA
- TP4 pad 1: /sensors/CLAMP_SENSOR -> /sensors/pressure_sensor/SENSOR_VOUT
- TP6 pad 1: /sensors/VAC_SENSOR -> /sensors/pressure_sensor1/SENSOR_VOUT
- U11 pad 14: /ADC-RESET -> /GPIO20
- U11 pad 15: /ADC-DRDY -> /GPIO3
- U11 pad 22: /RTC-INT -> /GPIO14
- U11 pad 23: /RTC-RESET -> /GPIO21
- U11 pad 26: /SOLENOID_6 -> /SOLENOID_1
- U11 pad 31: /SOLENOID_1 -> /SOLENOID_2
- U11 pad 32: /SOLENOID_2 -> /SOLENOID_3
- U11 pad 33: /SOLENOID_3 -> /SOLENOID_4
- U11 pad 34: /SOLENOID_4 -> /SOLENOID_5
- U11 pad 35: /SOLENOID_5 -> /SOLENOID_6
- U11 pad 8: /PUMP-IN2 -> /PUMP-IN1
- U11 pad 9: /PUMP-IN1 -> /PUMP-IN2
- U2 pad 1: GND -> +5V
- U2 pad 2: GND -> Net-(J3-Pin_2)
- U2 pad 3: /ADC-RESET -> Net-(J4-Pin_2)
- U2 pad 5: GNDA -> GND
- U2 pad 6: unconnected-(U2-AIN3-Pad6) -> /brushless_motor_pwm_driver/Pump_PWM
- U2 pad 7: unconnected-(U2-AIN2-Pad7) -> /brushless_motor_pwm_driver/Vac_PWM
- U2 pad 8: GNDA -> +3.3V
- U3 pad 6: /motor_driver1/MOTOR-OUT-1 -> Net-(J2-Pin_2)
- U3 pad 8: /motor_driver1/MOTOR-OUT-2 -> Net-(J2-Pin_1)
- U4 pad 1: +5V -> +5.5V
- U4 pad 3: +3.3V -> +5.5V
- U6 pad 1: +5.5V -> +3.3V
- U6 pad 2: GNDA -> GND
- U6 pad 3: +5.5V -> GNDA
- U6 pad 5: +5VA -> GND
- U8 pad 6: /motor_driver/MOTOR-OUT-1 -> Net-(J1-Pin_2)
- U8 pad 8: /motor_driver/MOTOR-OUT-2 -> Net-(J1-Pin_1)
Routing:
- net +24V: track 6.40 -> 217.1 mm, vias 57 -> 0
- net GND: track 27.4 -> 142.6 mm, vias 151 -> 64
- net /I2C-SDA: track 91.8 -> 19.8 mm, vias 4 -> 1
- net +5V: track 188.0 -> 116.9 mm, vias 3 -> 2
- net /I2C-SCL: track 88.1 -> 21.4 mm, vias 4 -> 1
- net /DISP-CS: track 55.6 -> 5.57 mm, vias 2 -> 1
- net /DISP-DC: track 55.9 -> 7.68 mm, vias 2 -> 1
- net /sensors/VAC_SENSOR: track 44.4 -> 0.00 mm, vias 2 -> 0
- net /PUMP-IN1: track 73.1 -> 36.7 mm, vias 2 -> 0
- net /ESP32-S3/BOOT: track 51.4 -> 16.7 mm, vias 2 -> 1
- net /sensors/CLAMP_SENSOR: track 34.2 -> 0.00 mm
- net /RTC-RESET: track 32.7 -> 0.00 mm, vias 2 -> 0
- net +5.5V: track 71.8 -> 39.6 mm
- net /RTC-INT: track 28.3 -> 0.00 mm, vias 2 -> 0
- net /sensors/pressure_sensor/SENSOR_VOUT: track 0.00 -> 27.2 mm, vias 0 -> 1
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- added copper zone on F.Cu, net Net-(D8-K)
- removed copper zone on B.Cu, net +24V
- removed copper zone on B.Cu, net +5.5V
- removed copper zone on B.Cu, net GND
- removed copper zone on In1.Cu, net GNDA
- removed copper zone on In2.Cu, net GNDA
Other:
- board size 130 x 65 mm -> 95 x 70.5 mm
- board text removed: "+ - CLAMP"
- board text removed: "+ - VAC"
- board text removed: "+ PWM - CLAMP BLDC"
- board text removed: "+ PWM - VAC BLDC"
- board text removed: "- + S1"
- board text removed: "- + S2"
- board text removed: "- + S3"
- board text removed: "- + S4"
- board text removed: "- + S5"
- board text removed: "- + S6"
- board text removed: "P1 (+)"
- board text removed: "P2 (-)"
- board text removed: "PUMP"
- board text removed: "VAC"
